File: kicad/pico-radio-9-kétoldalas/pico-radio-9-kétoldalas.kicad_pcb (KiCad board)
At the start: 2 copper layers, 88 x 57.2 mm, 53 parts, among them J1 FM antenna, J2 SW antenna, J3 MW/SW antenna kapcsoló, J4 HF Amplifier, J5 Batterry, J6 KY-040 Rotary, Q1 PN2222A, Q2 PN2222A, Q3 PN2222A, SW1 Reset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

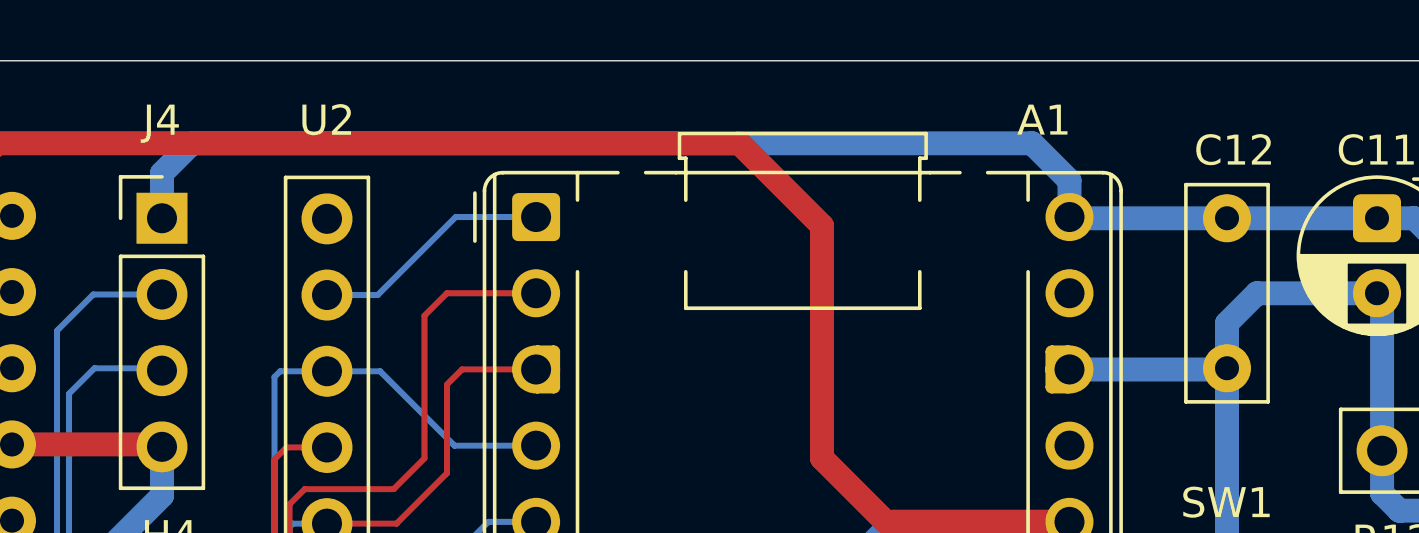
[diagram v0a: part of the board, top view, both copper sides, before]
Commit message: Vsys - Vbus power modification
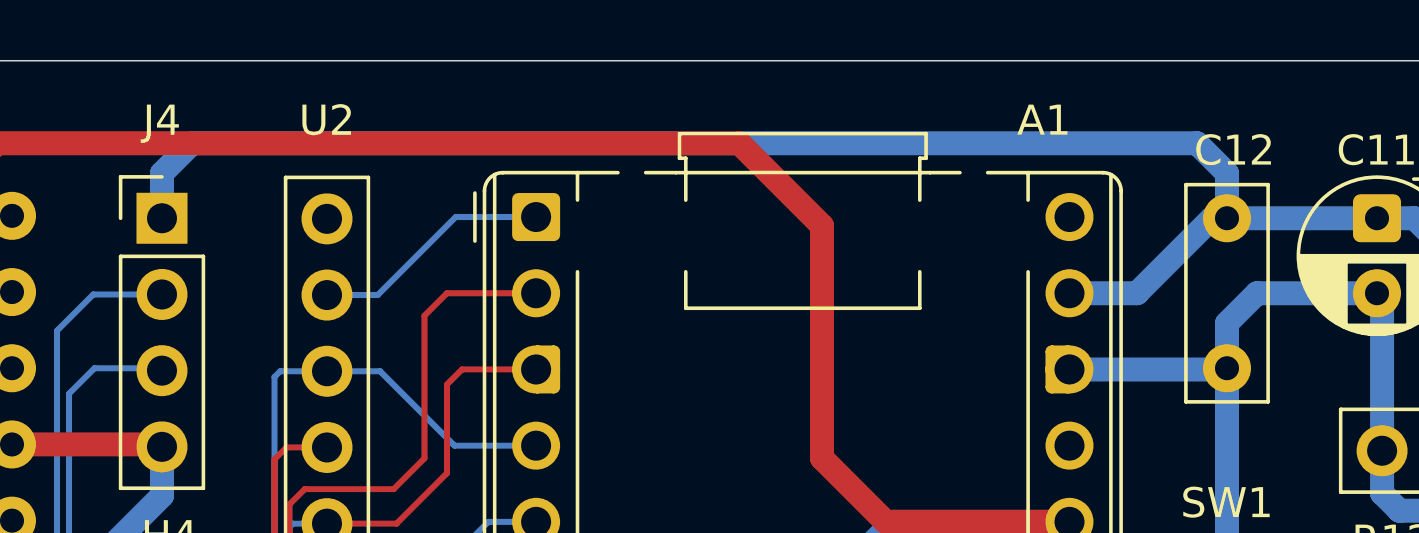
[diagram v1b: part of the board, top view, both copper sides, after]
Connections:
- A1 pad 40: +Vbus -> unconnected-(A1-VBUS-Pad40)
- BZ1 pad 1: +Vbus -> +Vsys
- C11 pad 1: +Vbus -> +Vsys
- C12 pad 1: +Vbus -> +Vsys
- J4 pad 1: +Vbus -> +Vsys
- J5 pad 2: +Vbus -> +Vsys
- R12 pad 1: +Vbus -> +Vsys
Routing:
- net +Vsys: track 0.00 -> 95.4 mm
- net +Vbus: track 89.0 -> 0.00 mm
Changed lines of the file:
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@@
 	(net 16 "BUZZER")
 	(net 17 "/RST")
-	(net 18 "+Vbus")
+	(net 18 "unconnected-(A1-VBUS-Pad40)")
 	(net 19 "/SDI")
 	(net 20 "unconnected-(A1-GPIO23-Pad26)")
@@
 			(layers "*.Cu" "*.Mask")
 			(remove_unused_layers no)
-			(net 18 "+Vbus")
+			(net 18 "unconnected-(A1-VBUS-Pad40)")
 			(pinfunction "VBUS")
-			(pintype "power_out")
+			(pintype "power_out+no_connect")
 		)
 		(group ""
@@
 			(layers "*.Cu" "*.Mask")
 			(remove_unused_layers no)
-			(net 18 "+Vbus")
+			(net 4 "+Vsys")
 			(pintype "passive")
 		)
@@
 			(layers "*.Cu" "*.Mask")
 			(remove_unused_layers no)
-			(net 18 "+Vbus")
+			(net 4 "+Vsys")
 			(pinfunction "+")
 			(pintype "passive")
@@
 			(layers "*.Cu" "*.Mask")
 			(remove_unused_layers no)
-			(net 18 "+Vbus")
+			(net 4 "+Vsys")
 			(pintype "passive")
 		)
@@
 			(layers "*.Cu" "*.Mask")
 			(remove_unused_layers no)
-			(net 18 "+Vbus")
+			(net 4 "+Vsys")
 			(pinfunction "Pin_2")
 			(pintype "passive")
@@
 			(layers "*.Cu" "*.Mask")
 			(remove_unused_layers no)
-			(net 18 "+Vbus")
+			(net 4 "+Vsys")
 			(pinfunction "Pin_1")
 			(pintype "passive")
@@
 			(remove_unused_layers no)
 			(roundrect_rratio 0.15625)
-			(net 18 "+Vbus")
+			(net 4 "+Vsys")
 			(pintype "passive")
 		)
@@
 	)
 	(segment
+		(start 135 47.84)
+		(end 135 61)
+		(width 0.8)
+		(layer "B.Cu")
+		(net 4)
+	)
+	(segment
+		(start 130.5 47.84)
+		(end 135 47.84)
+		(width 0.8)
+		(layer "B.Cu")
+		(net 4)
+	)
+	(segment
+		(start 124 32.75)
+		(end 125 33.75)
+		(width 0.8)
+		(layer "B.Cu")
+		(net 4)
+	)
+	(segment
+		(start 133.75 62.25)
+		(end 133.75 63.95)
+		(width 0.8)
+		(layer "B.Cu")
+		(net 4)
+	)
+	(segment
+		(start 90.5 32.75)
+		(end 124 32.75)
+		(width 0.8)
+		(layer "B.Cu")
+		(net 4)
+	)
+	(segment
+		(start 89.5 33.75)
+		(end 90.5 32.75)
+		(width 0.8)
+		(layer "B.Cu")
+		(net 4)
+	)
+	(segment
+		(start 135.25 47.84)
+		(end 137.75 45.34)
+		(width 0.8)
+		(layer "B.Cu")
+		(net 4)
+	)
+	(segment
+		(start 132.71 36.71)
+		(end 131.25 35.25)
+		(width 0.8)
+		(layer "B.Cu")
+		(net 4)
+	)
+	(segment
+		(start 131.25 35.25)
+		(end 129.75 35.25)
+		(width 0.8)
+		(layer "B.Cu")
+		(net 4)
+	)
+	(segment
+		(start 136.75 39.75)
+		(end 132.71 39.75)
+		(width 0.8)
+		(layer "B.Cu")
+		(net 4)
+	)
+	(segment
+		(start 137.75 40.75)
+		(end 136.75 39.75)
+		(width 0.8)
+		(layer "B.Cu")
+		(net 4)
+	)
+	(segment
+		(start 122 37.75)
+		(end 119.75 37.75)
+		(width 0.8)
+		(layer "B.Cu")
+		(net 4)
+	)
+	(segment
+		(start 130 35.25)
+		(end 125 35.25)
+		(width 0.8)
+		(layer "B.Cu")
+		(net 4)
+	)
+	(segment
+		(start 89.5 35.25)
+		(end 89.5 33.75)
+		(width 0.8)
+		(layer "B.Cu")
+		(net 4)
+	)
+	(segment
+		(start 135 61)
+		(end 133.75 62.25)
+		(width 0.8)
+		(layer "B.Cu")
+		(net 4)
+	)
+	(segment
+		(start 124.5 35.25)
+		(end 122 37.75)
+		(width 0.8)
+		(layer "B.Cu")
+		(net 4)
+	)
+	(segment
+		(start 135 47.84)
+		(end 135.25 47.84)
+		(width 0.8)
+		(layer "B.Cu")
+		(net 4)
+	)
+	(segment
+		(start 137.75 45.34)
+		(end 137.75 40.75)
+		(width 0.8)
+		(layer "B.Cu")
+		(net 4)
+	)
+	(segment
+		(start 125 35.25)
+		(end 124.5 35.25)
+		(width 0.8)
+		(layer "B.Cu")
+		(net 4)
+	)
+	(segment
+		(start 132.71 43)
+		(end 132.71 36.71)
+		(width 0.8)
+		(layer "B.Cu")
+		(net 4)
+	)
+	(segment
+		(start 125 33.75)
+		(end 125 35.25)
+		(width 0.8)
+		(layer "B.Cu")
+		(net 4)
+	)
+	(segment
 		(start 95 63.41)
 		(end 95.16 63.25)
@@
 	)
 	(segment
-		(start 135 47.84)
-		(end 135 61)
-		(width 0.8)
-		(layer "B.Cu")
-		(net 18)
-	)
-	(segment
-		(start 89.5 33.75)
-		(end 90.5 32.75)
-		(width 0.8)
-		(layer "B.Cu")
-		(net 18)
-	)
-	(segment
-		(start 130.5 47.84)
-		(end 135 47.84)
-		(width 0.8)
-		(layer "B.Cu")
-		(net 18)
-	)
-	(segment
-		(start 90.5 32.75)
-		(end 118.5 32.75)
-		(width 0.8)
-		(layer "B.Cu")
-		(net 18)
-	)
-	(segment
-		(start 118.5 32.75)
-		(end 119.75 34)
-		(width 0.8)
-		(layer "B.Cu")
-		(net 18)
-	)
-	(segment
-		(start 133.75 62.25)
-		(end 133.75 63.95)
-		(width 0.8)
-		(layer "B.Cu")
-		(net 18)
-	)
-	(segment
-		(start 135.25 47.84)
-		(end 137.75 45.34)
-		(width 0.8)
-		(layer "B.Cu")
-		(net 18)
-	)
-	(segment
-		(start 132.71 36.71)
-		(end 131.25 35.25)
-		(width 0.8)
-		(layer "B.Cu")
-		(net 18)
-	)
-	(segment
-		(start 125 35.25)
-		(end 119.79 35.25)
-		(width 0.8)
-		(layer "B.Cu")
-		(net 18)
-	)
-	(segment
-		(start 119.75 34)
-		(end 119.75 35.21)
-		(width 0.8)
-		(layer "B.Cu")
-		(net 18)
-	)
-	(segment
-		(start 131.25 35.25)
-		(end 129.75 35.25)
-		(width 0.8)
-		(layer "B.Cu")
-		(net 18)
-	)
-	(segment
-		(start 136.75 39.75)
-		(end 132.71 39.75)
-		(width 0.8)
-		(layer "B.Cu")
-		(net 18)
-	)
-	(segment
-		(start 137.75 40.75)
-		(end 136.75 39.75)
-		(width 0.8)
-		(layer "B.Cu")
-		(net 18)
-	)
-	(segment
-		(start 130 35.25)
-		(end 125 35.25)
-		(width 0.8)
-		(layer "B.Cu")
-		(net 18)
-	)
-	(segment
-		(start 135 61)
-		(end 133.75 62.25)
-		(width 0.8)
-		(layer "B.Cu")
-		(net 18)
-	)
-	(segment
 		(start 119.79 35.25)
 		(end 119.75 35.21)
 		(width 0.8)
 		(layer "B.Cu")
-		(net 18)
-	)
-	(segment
-		(start 135 47.84)
-		(end 135.25 47.84)
-		(width 0.8)
-		(layer "B.Cu")
-		(net 18)
-	)
-	(segment
-		(start 89.5 35.25)
-		(end 89.5 33.75)
-		(width 0.8)
-		(layer "B.Cu")
-		(net 18)
-	)
-	(segment
-		(start 137.75 45.34)
-		(end 137.75 40.75)
-		(width 0.8)
-		(layer "B.Cu")
-		(net 18)
-	)
-	(segment
-		(start 132.71 43)
-		(end 132.71 36.71)
-		(width 0.8)
-		(layer "B.Cu")

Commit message: Add capacitors C13 and C14 to the schematic and update connections
- Added capacitor C13 (100nF) at coordinates (96.52, 148.59) with appropriate properties.
- Added capacitor C14 (100nF) at coordinates (96.52, 171.45) with appropriate properties.
- Updated wire connections for C13 and C14.
- Changed the value of resistor R1 from 100k to 47k.
- Adjusted the position of capacitor C7 for better layout.
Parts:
- added C13: 100nF, Capacitor_THT:C_Disc_D5.0mm_W2.5mm_P2.50mm, F.Cu at (68.0, 48.5)
- added C14: 100nF, Capacitor_THT:C_Disc_D5.0mm_W2.5mm_P2.50mm, F.Cu at (71.2, 48.5)
- C9: value 100nF -> 470nF
- R11: value 100k -> 47k
- R5, R7: footprint Resistor_THT:R_Axial_DIN0207_L6.3mm_D2.5mm_P10.16mm_Horizontal -> Resistor_THT:R_Axial_DIN0207_L6.3mm_D2.5mm_P2.54mm_Vertical
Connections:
- R5 pad 2: AUDIO_R -> Net-(C13-Pad1)
- R7 pad 2: AUDIO_L -> Net-(C14-Pad1)
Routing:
- net Net-(C14-Pad1): track 0.00 -> 5.96 mm
- net Net-(C13-Pad1): track 0.00 -> 5.96 mm
- net AUDIO_R: track 59.0 -> 58.1 mm
- net AUDIO_L: track 60.7 -> 60.0 mm
- net Net-(U3B--): track 24.1 -> 24.7 mm
